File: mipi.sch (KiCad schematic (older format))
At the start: 4 parts, among them Q2001 FDV301N, Q2002 FDV301N

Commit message: Modify the boot config/boot mode pins and switch such that only eMMC and USB (serial downloader) are boot options due to the uSD being attached to the USB<->SD bridge chip, add OV5460 notes about using the internal DVDD 1.5V regulator
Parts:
- renumbered Q2001 to Q1101, Q2002 to Q1102, R2004 to R1101, R2005 to R1102
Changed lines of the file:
@@
 I2C1_SCL
 $Comp
-L Q_NMOS_SGD Q2001
+L Q_NMOS_SGD Q1101
 U 1 1 5B1803E8
 P 7950 3200
-F 0 "Q2001" V 8200 3100 50  0000 L CNN
+F 0 "Q1101" V 8200 3100 50  0000 L CNN
 F 1 "FDV301N" V 8300 3050 50  0000 L CNN
 F 2 "" H 8150 3300 50  0001 C CNN
@@
 $EndComp
 $Comp
-L 1V8_P #PWR0167
+L 1V8_P #PWR0161
 U 1 1 5B1803EF
 P 7700 2850
-F 0 "#PWR0167" H 7700 2700 50  0001 C CNN
+F 0 "#PWR0161" H 7700 2700 50  0001 C CNN
 F 1 "1V8_P" H 7700 2990 50  0000 C CNN
 F 2 "" H 7700 2850 50  0001 C CNN
@@
 $EndComp
 $Comp
-L Q_NMOS_SGD Q2002
+L Q_NMOS_SGD Q1102
 U 1 1 5B1803F6
 P 7950 4150
-F 0 "Q2002" V 8200 4050 50  0000 L CNN
+F 0 "Q1102" V 8200 4050 50  0000 L CNN
 F 1 "FDV301N" V 8300 4000 50  0000 L CNN
 F 2 "" H 8150 4250 50  0001 C CNN
@@
 $EndComp
 $Comp
-L 1V8_P #PWR0168
+L 1V8_P #PWR0162
 U 1 1 5B180400
 P 7700 3800
-F 0 "#PWR0168" H 7700 3650 50  0001 C CNN
+F 0 "#PWR0162" H 7700 3650 50  0001 C CNN
 F 1 "1V8_P" H 7700 3940 50  0000 C CNN
 F 2 "" H 7700 3800 50  0001 C CNN
@@
 Connection ~ 7700 3850
 $Comp
-L R R2004
+L R R1101
 U 1 1 5B18041B
 P 7700 3100
-F 0 "R2004" H 7875 3150 50  0000 C CNN
+F 0 "R1101" H 7875 3150 50  0000 C CNN
 F 1 "10k" H 7825 3050 50  0000 C CNN
 F 2 "Resistors_SMD:R_0603" V 7630 3100 50  0001 C CNN
@@
 $EndComp
 $Comp
-L R R2005
+L R R1102
 U 1 1 5B180428
 P 7700 4050
-F 0 "R2005" H 7875 4100 50  0000 C CNN
+F 0 "R1102" H 7875 4100 50  0000 C CNN
 F 1 "10k" H 7825 4000 50  0000 C CNN
 F 2 "Resistors_SMD:R_0603" V 7630 4050 50  0001 C CNN

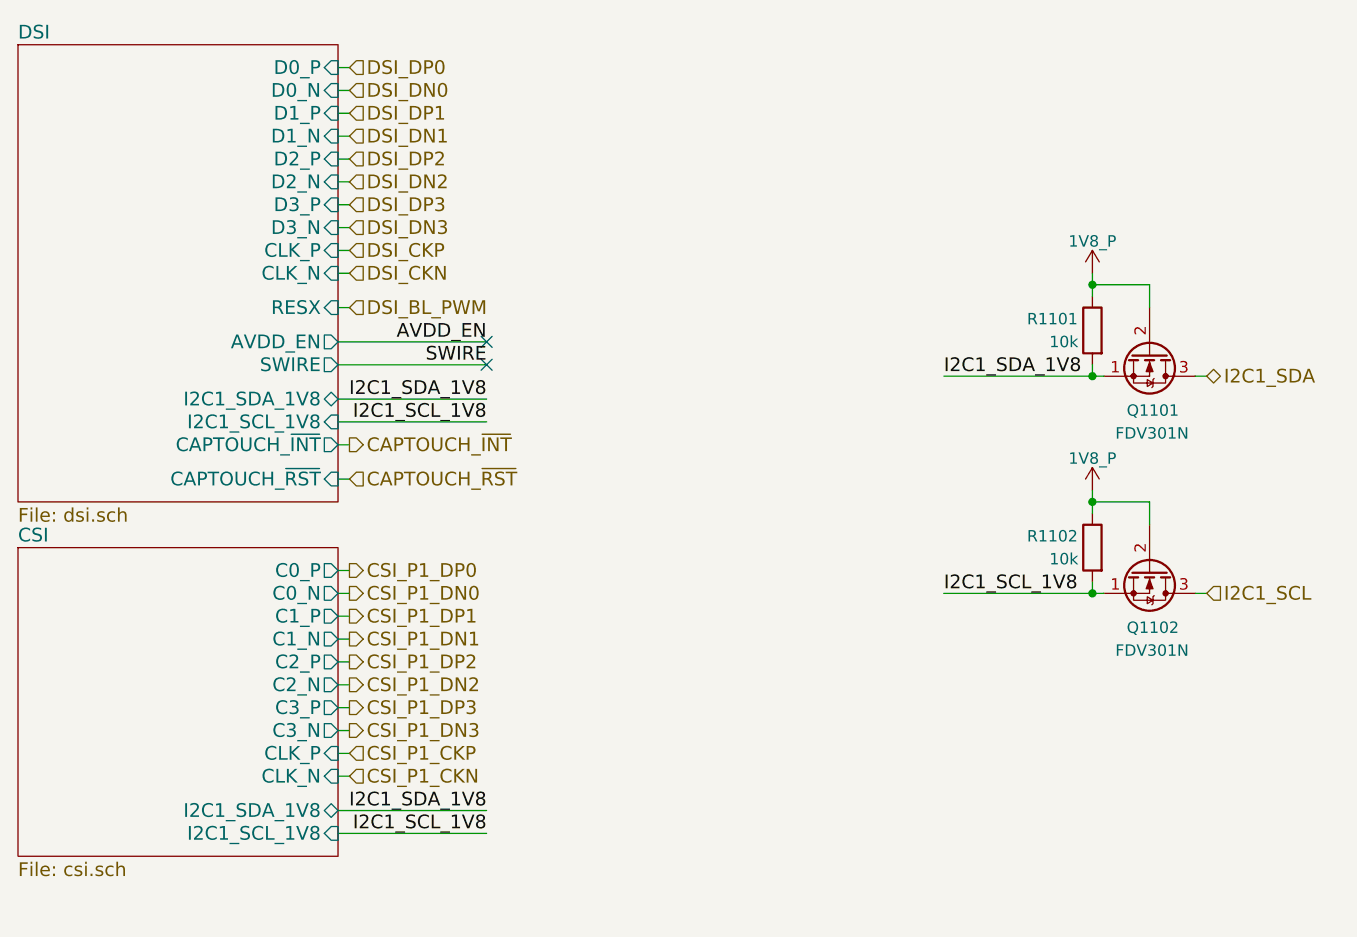
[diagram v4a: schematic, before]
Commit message: Add LCD display's 22.4V (@40mA) LED backlight driver/boost converter IC circuit (PAM2841), selected the rectifying/schottky diode (SS14), and set the OVP to 37.6V as found on the IC's EVB
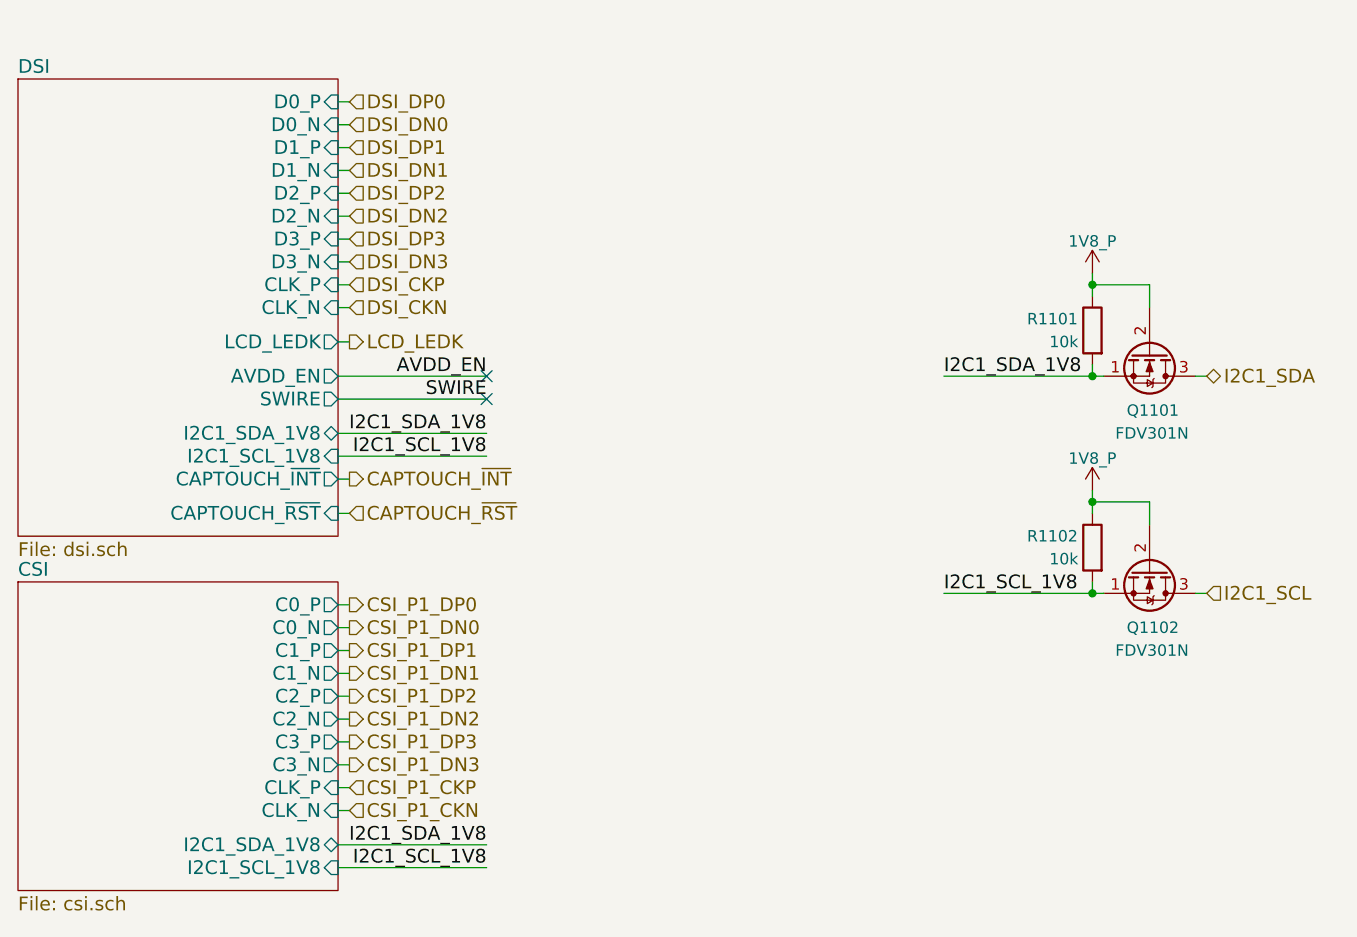
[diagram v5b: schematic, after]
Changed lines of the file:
@@
 $EndDescr
 $Sheet
-S 3000 1850 1400 2000
+S 3000 2000 1400 2000
 U 5B12DFA8
 F0 "DSI" 60
 F1 "dsi.sch" 60
-F2 "D2_P" I R 4400 2350 60
-F3 "D2_N" I R 4400 2450 60
-F4 "D1_P" I R 4400 2150 60
-F5 "D1_N" I R 4400 2250 60
-F6 "CLK_P" I R 4400 2750 60
-F7 "CLK_N" I R 4400 2850 60
-F8 "D0_P" I R 4400 1950 60
-F9 "D0_N" I R 4400 2050 60
-F10 "D3_P" I R 4400 2550 60
-F11 "D3_N" I R 4400 2650 60
-F12 "CAPTOUCH_~INT" O R 4400 3600 60
-F13 "CAPTOUCH_~RST" I R 4400 3750 60
-F14 "AVDD_EN" O R 4400 3150 60
-F15 "SWIRE" O R 4400 3250 60
-F16 "RESX" I R 4400 3000 60
-F17 "I2C1_SDA_1V8" B R 4400 3400 60
-F18 "I2C1_SCL_1V8" I R 4400 3500 60
+F2 "D2_P" I R 4400 2500 60
+F3 "D2_N" I R 4400 2600 60
+F4 "D1_P" I R 4400 2300 60
+F5 "D1_N" I R 4400 2400 60
+F6 "CLK_P" I R 4400 2900 60
+F7 "CLK_N" I R 4400 3000 60
+F8 "D0_P" I R 4400 2100 60
+F9 "D0_N" I R 4400 2200 60
+F10 "D3_P" I R 4400 2700 60
+F11 "D3_N" I R 4400 2800 60
+F12 "CAPTOUCH_~INT" O R 4400 3750 60
+F13 "CAPTOUCH_~RST" I R 4400 3900 60
+F14 "AVDD_EN" O R 4400 3300 60
+F15 "SWIRE" O R 4400 3400 60
+F16 "I2C1_SDA_1V8" B R 4400 3550 60
+F17 "I2C1_SCL_1V8" I R 4400 3650 60
+F18 "LCD_LEDK" O R 4400 3150 60
 $EndSheet
-Text Label 5050 3150 2    60   ~ 0
+Text Label 5050 3300 2    60   ~ 0
 AVDD_EN
-Text Label 5050 3250 2    60   ~ 0
+Text Label 5050 3400 2    60   ~ 0
 SWIRE
-Text Label 5050 3400 2    60   ~ 0
+Text Label 5050 3550 2    60   ~ 0
 I2C1_SDA_1V8
-Text Label 5050 3500 2    60   ~ 0
+Text Label 5050 3650 2    60   ~ 0
 I2C1_SCL_1V8
-NoConn ~ 5050 3250
-NoConn ~ 5050 3150
-Wire Wire Line
-	4400 4650 4450 4650
-Wire Wire Line
-	4400 5050 4450 5050
-Wire Wire Line
-	4400 4950 4450 4950
-Wire Wire Line
-	4400 4250 4450 4250
-Wire Wire Line
-	4400 4150 4450 4150
-Wire Wire Line
-	4400 4550 4450 4550
-Wire Wire Line
-	4400 4450 4450 4450
-Wire Wire Line
-	4400 4350 4450 4350
-Wire Wire Line
-	4400 4850 4450 4850
-Wire Wire Line
-	4400 4750 4450 4750
+NoConn ~ 5050 3400
+NoConn ~ 5050 3300
+Wire Wire Line
+	4400 4800 4450 4800
+Wire Wire Line
+	4400 5200 4450 5200
+Wire Wire Line
+	4400 5100 4450 5100
+Wire Wire Line
+	4400 4400 4450 4400
+Wire Wire Line
+	4400 4300 4450 4300
+Wire Wire Line
+	4400 4700 4450 4700
+Wire Wire Line
+	4400 4600 4450 4600
+Wire Wire Line
+	4400 4500 4450 4500
+Wire Wire Line
+	4400 5000 4450 5000
+Wire Wire Line
+	4400 4900 4450 4900
 Wire Wire Line
 	4400 3750 4450 3750
 Wire Wire Line
-	4400 3600 4450 3600
-Wire Wire Line
-	4400 3500 5050 3500
+	4400 3650 5050 3650
+Wire Wire Line
+	4400 3550 5050 3550
 Wire Wire Line
 	4400 3400 5050 3400
 Wire Wire Line
-	4400 3250 5050 3250
-Wire Wire Line
-	4400 3150 5050 3150
-Wire Wire Line
-	4400 2850 4450 2850
-Wire Wire Line
-	4400 2750 4450 2750
-Wire Wire Line
-	4400 2650 4450 2650
-Wire Wire Line
-	4400 2550 4450 2550
-Wire Wire Line
-	4400 2450 4450 2450
-Wire Wire Line
-	4400 2350 4450 2350
-Wire Wire Line
-	4400 2250 4450 2250
-Wire Wire Line
-	4400 2150 4450 2150
-Wire Wire Line
-	4400 2050 4450 2050
-Wire Wire Line
-	4400 1950 4450 1950
-Text HLabel 4450 1950 2    60   Input ~ 0
+	4400 3300 5050 3300
+Wire Wire Line
+	4400 3000 4450 3000
+Wire Wire Line
+	4400 2900 4450 2900
+Wire Wire Line
+	4400 2800 4450 2800
+Wire Wire Line
+	4400 2700 4450 2700
+Wire Wire Line
+	4400 2600 4450 2600
+Wire Wire Line
+	4400 2500 4450 2500
+Wire Wire Line
+	4400 2400 4450 2400
+Wire Wire Line
+	4400 2300 4450 2300
+Wire Wire Line
+	4400 2200 4450 2200
+Wire Wire Line
+	4400 2100 4450 2100
+Text HLabel 4450 2100 2    60   Input ~ 0
 DSI_DP0
-Text HLabel 4450 2150 2    60   Input ~ 0
+Text HLabel 4450 2300 2    60   Input ~ 0
 DSI_DP1
-Text HLabel 4450 2350 2    60   Input ~ 0
+Text HLabel 4450 2500 2    60   Input ~ 0
 DSI_DP2
-Text HLabel 4450 2550 2    60   Input ~ 0
+Text HLabel 4450 2700 2    60   Input ~ 0
 DSI_DP3
-Text HLabel 4450 2050 2    60   Input ~ 0
+Text HLabel 4450 2200 2    60   Input ~ 0
 DSI_DN0
-Text HLabel 4450 2250 2    60   Input ~ 0
+Text HLabel 4450 2400 2    60   Input ~ 0
 DSI_DN1
-Text HLabel 4450 2450 2    60   Input ~ 0
+Text HLabel 4450 2600 2    60   Input ~ 0
 DSI_DN2
-Text HLabel 4450 2650 2    60   Input ~ 0
+Text HLabel 4450 2800 2    60   Input ~ 0
 DSI_DN3
-Text HLabel 4450 4150 2    60   Output ~ 0
+Text HLabel 4450 4300 2    60   Output ~ 0
 CSI_P1_DP0
-Text HLabel 4450 4350 2    60   Output ~ 0
+Text HLabel 4450 4500 2    60   Output ~ 0
 CSI_P1_DP1
-Text HLabel 4450 4550 2    60   Output ~ 0
+Text HLabel 4450 4700 2    60   Output ~ 0
 CSI_P1_DP2
-Text HLabel 4450 4750 2    60   Output ~ 0
+Text HLabel 4450 4900 2    60   Output ~ 0
 CSI_P1_DP3
-Text HLabel 4450 4250 2    60   Output ~ 0
+Text HLabel 4450 4400 2    60   Output ~ 0
 CSI_P1_DN0
-Text HLabel 4450 4450 2    60   Output ~ 0
+Text HLabel 4450 4600 2    60   Output ~ 0
 CSI_P1_DN1
-Text HLabel 4450 4650 2    60   Output ~ 0
+Text HLabel 4450 4800 2    60   Output ~ 0
 CSI_P1_DN2
-Text HLabel 4450 4850 2    60   Output ~ 0
+Text HLabel 4450 5000 2    60   Output ~ 0
 CSI_P1_DN3
-Text HLabel 4450 2750 2    60   Input ~ 0
+Text HLabel 4450 2900 2    60   Input ~ 0
 DSI_CKP
-Text HLabel 4450 2850 2    60   Input ~ 0
+Text HLabel 4450 3000 2    60   Input ~ 0
 DSI_CKN
-Text HLabel 4450 4950 2    60   Input ~ 0
+Text HLabel 4450 5100 2    60   Input ~ 0
 CSI_P1_CKP
-Text HLabel 4450 5050 2    60   Input ~ 0
+Text HLabel 4450 5200 2    60   Input ~ 0
 CSI_P1_CKN
-Text Label 5050 5200 2    60   ~ 0
+Text Label 5050 5350 2    60   ~ 0
 I2C1_SDA_1V8
-Text Label 5050 5300 2    60   ~ 0
+Text Label 5050 5450 2    60   ~ 0
 I2C1_SCL_1V8
 Wire Wire Line
-	4400 5300 5050 5300
-Wire Wire Line
-	4400 5200 5050 5200
+	4400 5450 5050 5450
+Wire Wire Line
+	4400 5350 5050 5350
 Text HLabel 8200 3300 2    60   BiDi ~ 0
 I2C1_SDA
@@
 $EndComp
 $Comp
-L 1V8_P #PWR0161
+L 1V8_P #PWR0172
 U 1 1 5B1803EF
 P 7700 2850
-F 0 "#PWR0161" H 7700 2700 50  0001 C CNN
+F 0 "#PWR0172" H 7700 2700 50  0001 C CNN
 F 1 "1V8_P" H 7700 2990 50  0000 C CNN
 F 2 "" H 7700 2850 50  0001 C CNN
@@
 $EndComp
 $Comp
-L 1V8_P #PWR0162
+L 1V8_P #PWR0173
 U 1 1 5B180400
 P 7700 3800
-F 0 "#PWR0162" H 7700 3650 50  0001 C CNN
+F 0 "#PWR0173" H 7700 3650 50  0001 C CNN
 F 1 "1V8_P" H 7700 3940 50  0000 C CNN
 F 2 "" H 7700 3800 50  0001 C CNN
@@
 Text Label 7050 4250 0    60   ~ 0
 I2C1_SCL_1V8
-Text HLabel 4450 3000 2    60   Input ~ 0
-DSI_BL_PWM
-Wire Wire Line
-	4450 3000 4400 3000
-Text HLabel 4450 3600 2    60   Output ~ 0
+Text HLabel 4450 3750 2    60   Output ~ 0
 CAPTOUCH_~INT
-Text HLabel 4450 3750 2    60   Input ~ 0
+Text HLabel 4450 3900 2    60   Input ~ 0
 CAPTOUCH_~RST
 $Sheet
-S 3000 4050 1400 1350
+S 3000 4200 1400 1350
 U 5B12DFE7
 F0 "CSI" 60
 F1 "csi.sch" 60
-F2 "C0_P" O R 4400 4150 60
-F3 "C0_N" O R 4400 4250 60
-F4 "C1_P" O R 4400 4350 60
-F5 "C1_N" O R 4400 4450 60
-F6 "C2_P" O R 4400 4550 60
-F7 "C2_N" O R 4400 4650 60
-F8 "C3_P" O R 4400 4750 60
-F9 "C3_N" O R 4400 4850 60
-F10 "CLK_P" I R 4400 4950 60
-F11 "CLK_N" I R 4400 5050 60
-F12 "I2C1_SDA_1V8" B R 4400 5200 60
-F13 "I2C1_SCL_1V8" I R 4400 5300 60
+F2 "C0_P" O R 4400 4300 60
+F3 "C0_N" O R 4400 4400 60
+F4 "C1_P" O R 4400 4500 60
+F5 "C1_N" O R 4400 4600 60
+F6 "C2_P" O R 4400 4700 60
+F7 "C2_N" O R 4400 4800 60
+F8 "C3_P" O R 4400 4900 60
+F9 "C3_N" O R 4400 5000 60
+F10 "CLK_P" I R 4400 5100 60
+F11 "CLK_N" I R 4400 5200 60
+F12 "I2C1_SDA_1V8" B R 4400 5350 60
+F13 "I2C1_SCL_1V8" I R 4400 5450 60
 $EndSheet
+Wire Wire Line
+	4400 3150 4450 3150
+Text HLabel 4450 3150 2    60   Output ~ 0
+LCD_LEDK
+Wire Wire Line
+	4450 3900 4400 3900
 $EndSCHEMATC
